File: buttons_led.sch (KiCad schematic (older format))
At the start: 13 parts, among them Q1301 2N7002P, SW1301 SW_Push, SW1302 SW_Push, SW1303 SW_Push, SW1304 SW_Push, SW1305 SW_Push

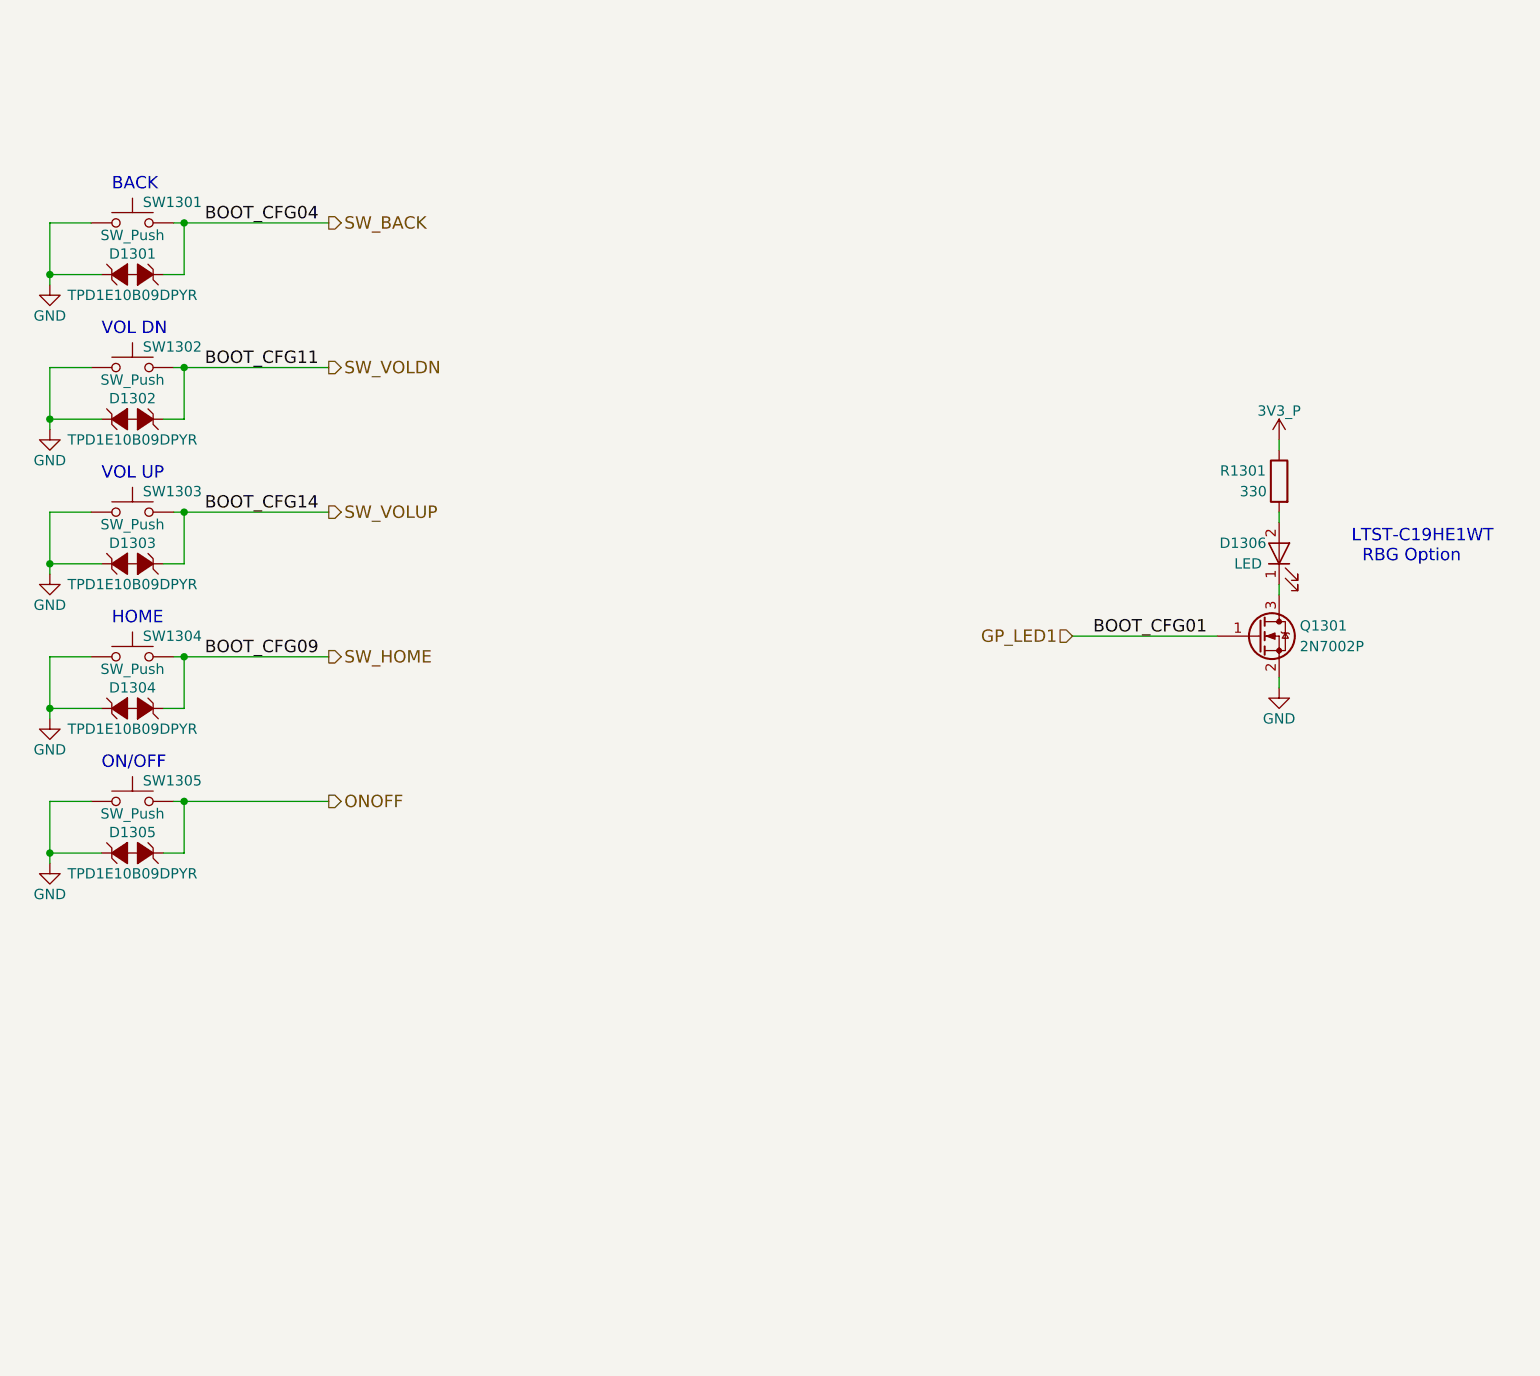
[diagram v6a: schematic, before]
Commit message: Modify the boot config pins such that the eMMC is an 8-bit bus, depressing a momentary push button switch during boot causes SD boot, and relevant options
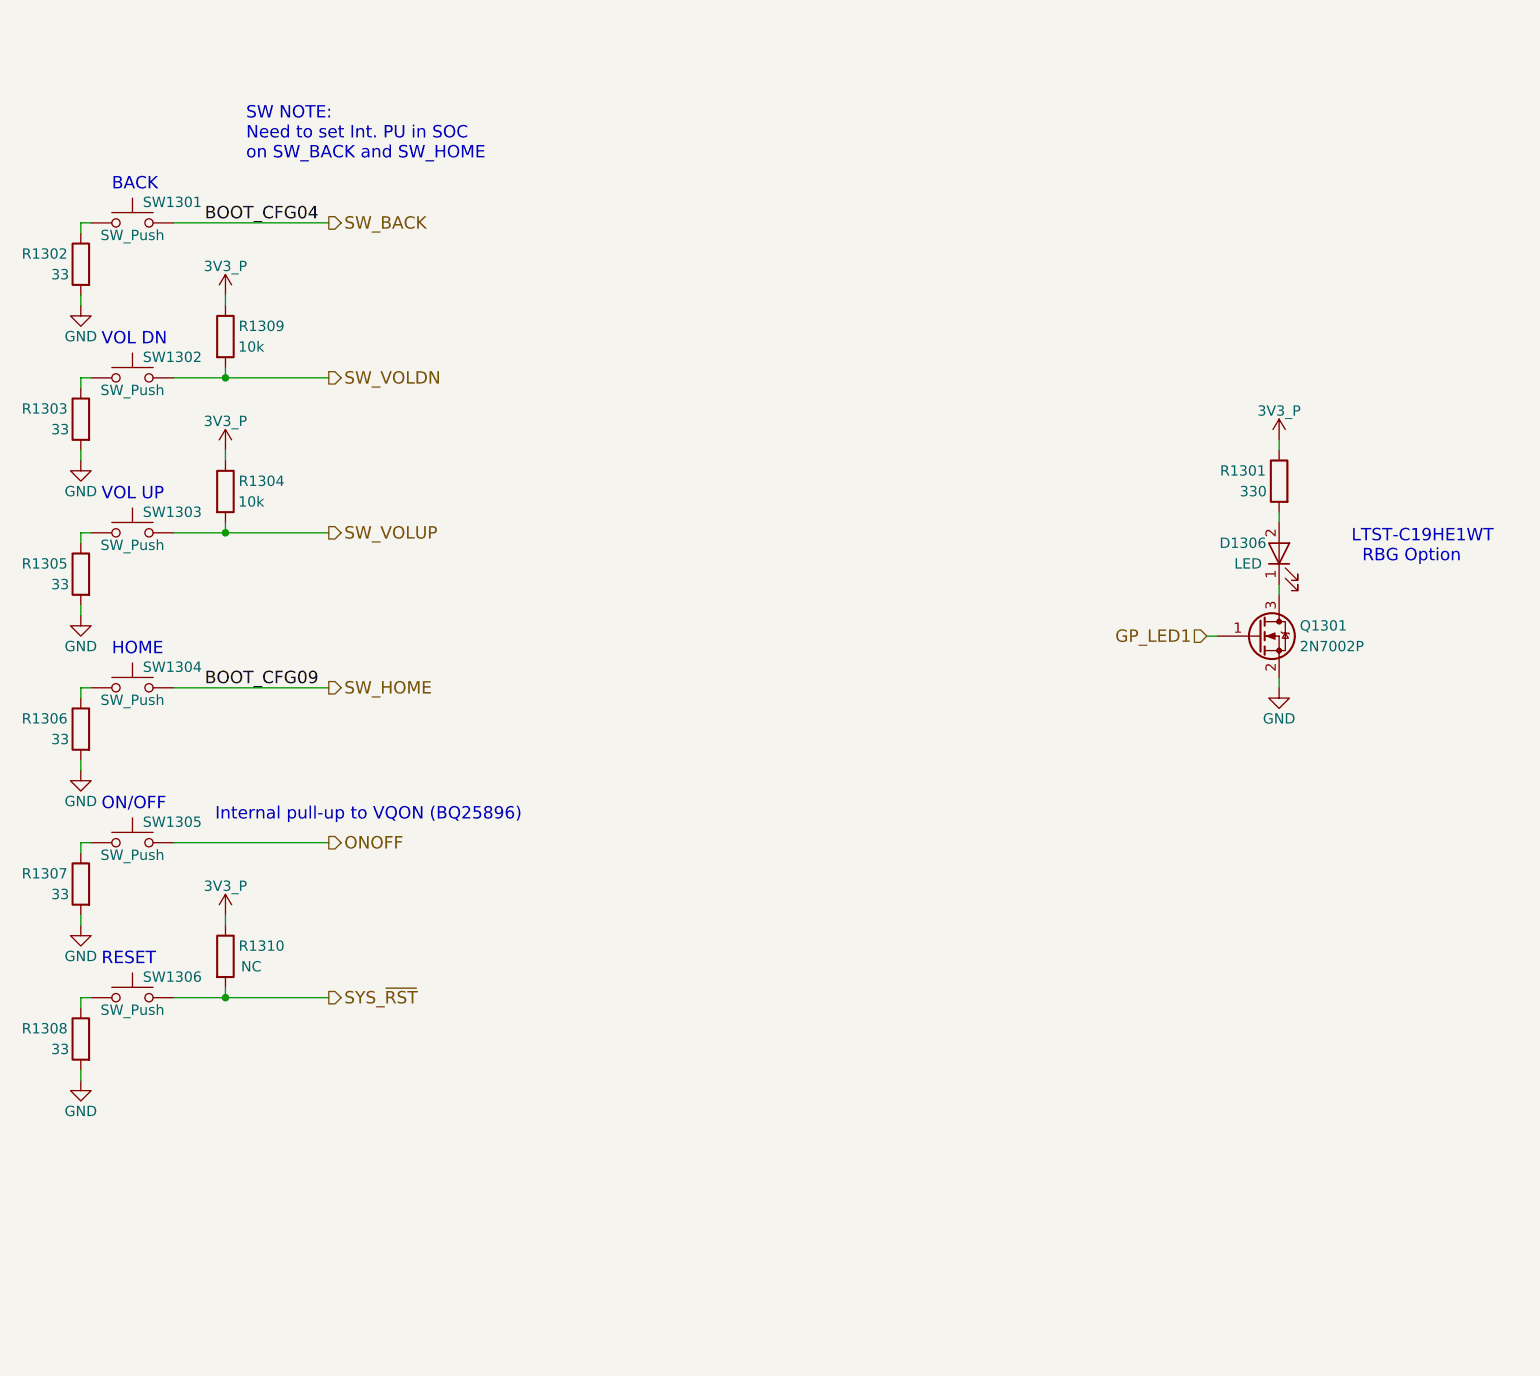
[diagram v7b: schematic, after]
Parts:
- removed D1301, D1302, D1303, D1304, D1305: TPD1E10B09DPYR, symbol TVS_DIODE
- added R1302, R1303, R1305, R1306, R1307, R1308: 33, symbol R
- added R1304, R1309: 10k, symbol R
- added R1310: NC, symbol R
- added SW1306: SW_Push, symbol SW_Push
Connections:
- net 3V3_P: now also R1304.1, R1309.1, R1310.1
- net GND: now also R1302.2, R1303.2, R1305.2, R1306.2, R1307.2, R1308.2; no longer SW1301.1, SW1302.1, SW1303.1, SW1304.1, SW1305.1
- net SW_VOLDN: now also R1309.2
- net SW_VOLUP: now also R1304.2
- new net: R1302.1, SW1301.1
- new net: R1303.1, SW1302.1
- new net: R1305.1, SW1303.1
- new net: R1306.1, SW1304.1
- new net: R1307.1, SW1305.1
- new net: R1308.1, SW1306.1
- new net SYS_~RST: R1310.2, SW1306.2
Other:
- note added: "Internal pull-up to VQON (BQ25896)"
- note added: "RESET"
- note added: "SW NOTE:\nNeed to set Int. PU in SOC\non SW_BACK and SW_HOME"
- moved on the sheet: SW1302, SW1303, SW1304, SW1305

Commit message: Begin USB 2.0 hub circuit for M.2 modules, remove supervisory/voltage monitor/watchdog circuit since the EmCraft SoM implements it
USB 2.0 hub circuit still needs to be completed.
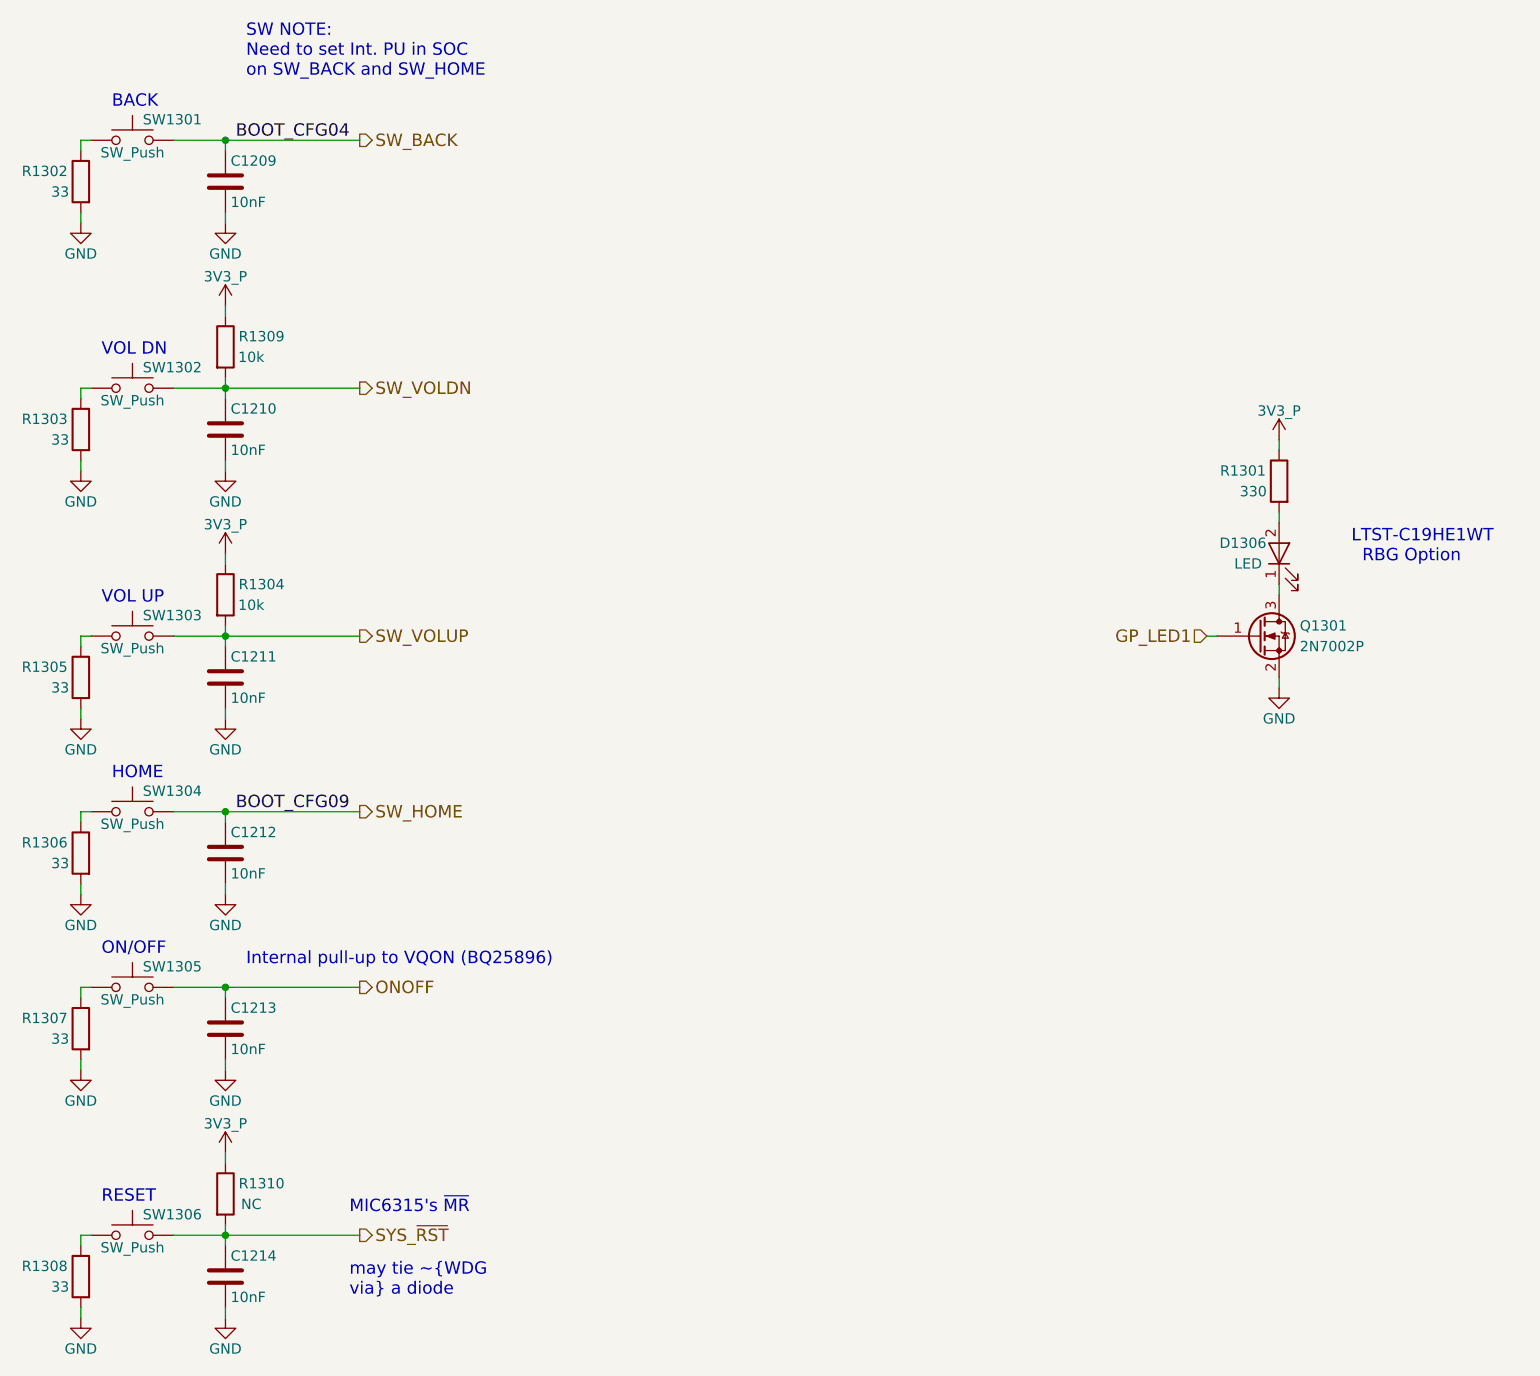
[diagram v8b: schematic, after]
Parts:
- added C1209, C1210, C1211, C1212, C1213, C1214: 10nF, symbol C
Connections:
- net GND: now also C1209.2, C1210.2, C1211.2, C1212.2, C1213.2, C1214.2
- net ONOFF: now also C1213.1
- net SW_BACK: now also C1209.1
- net SW_HOME: now also C1212.1
- net SW_VOLDN: now also C1210.1
- net SW_VOLUP: now also C1211.1
- net SYS_~RST: now also C1214.1
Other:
- note added: "MIC6315's ~MR"
- note added: "may tie ~WDG\nvia a diode"
- moved on the sheet: R1302, R1303, R1304, R1305, R1306, R1307, R1308, R1309, R1310, SW1301, SW1302, SW1303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
